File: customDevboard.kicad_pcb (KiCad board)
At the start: 4 copper layers, 40 x 81 mm, 76 parts, among them J1 From BEC, J2 USB_C_Receptacle_USB2.0_14P, J3 From BEC, J4 From Battery, U1 DPS310, U3 TPD2EUSB30, U4 TPS5430DDA, U5 STM32F722RET6, U6 TLV75733PDRV, U7 BMI270, Y1 8MHz, Y2 32.768KHz

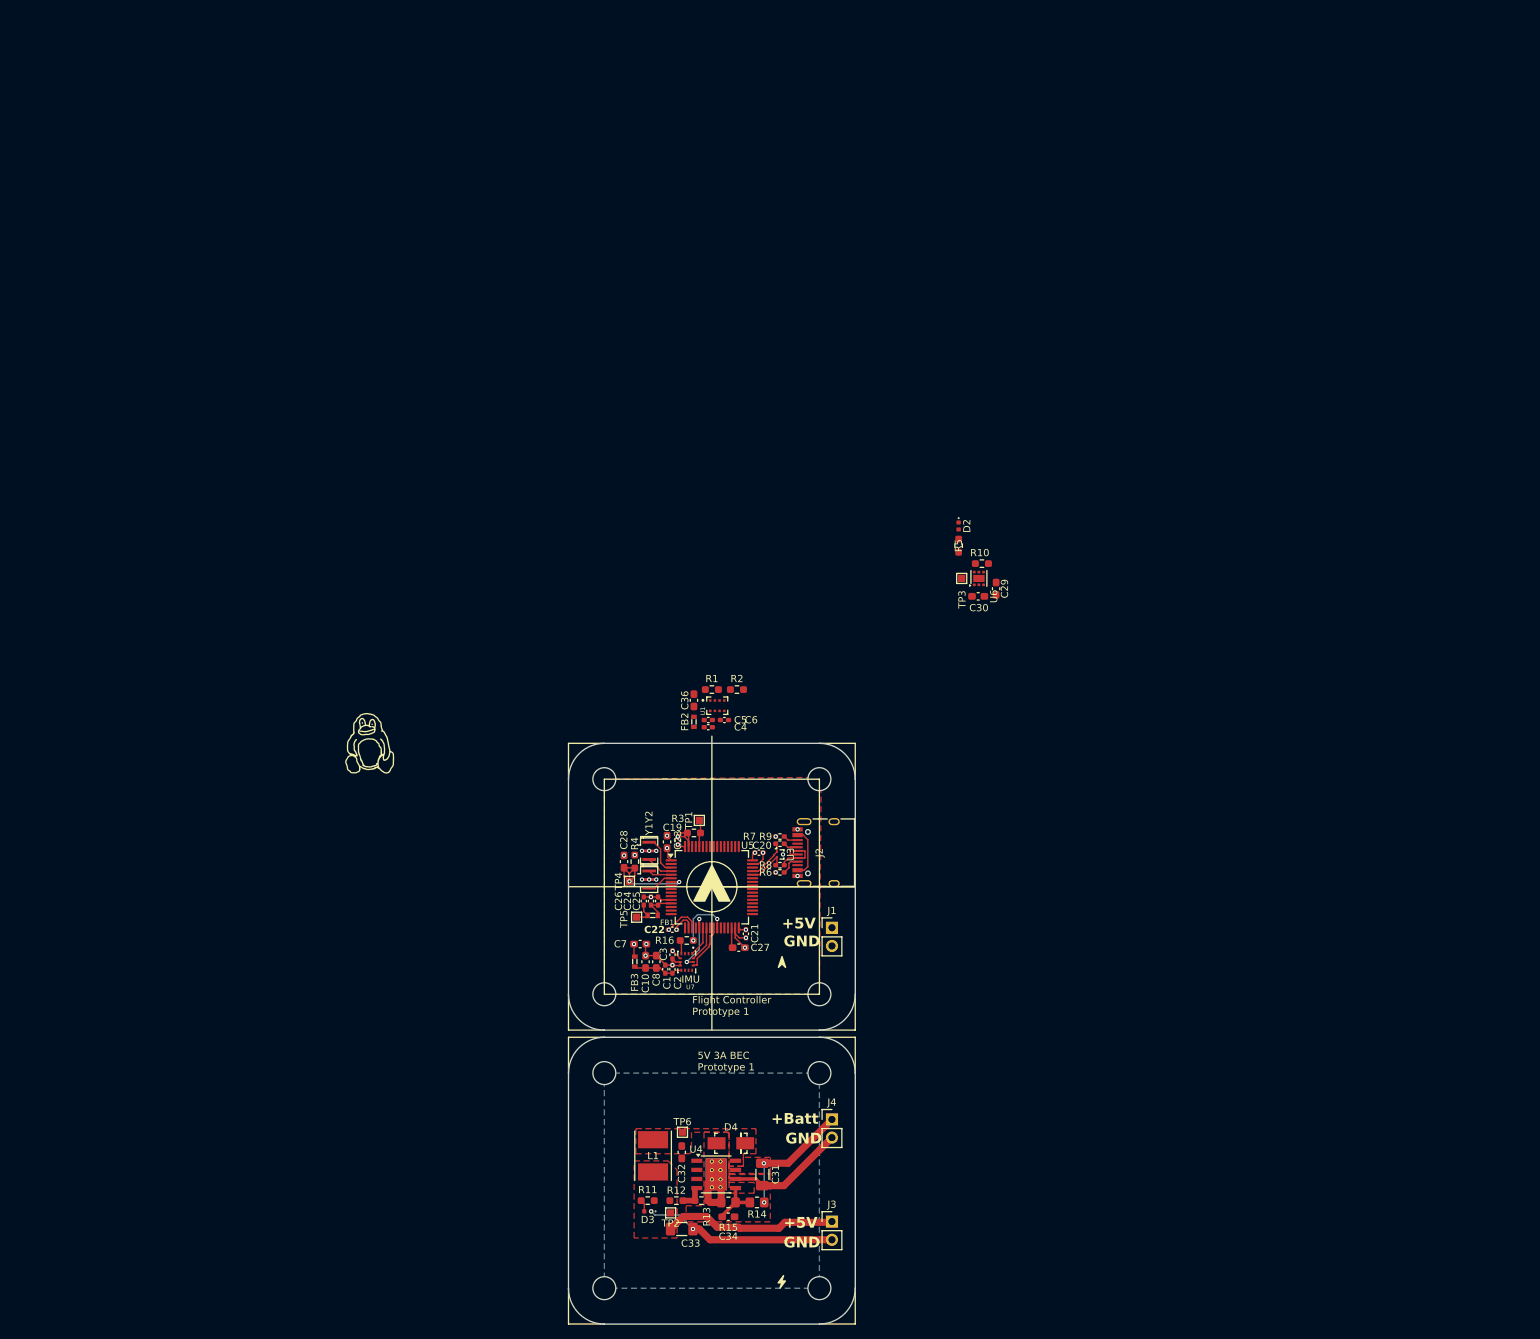
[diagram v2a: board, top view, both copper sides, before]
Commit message: prepare to move esc, gps, bec to other project
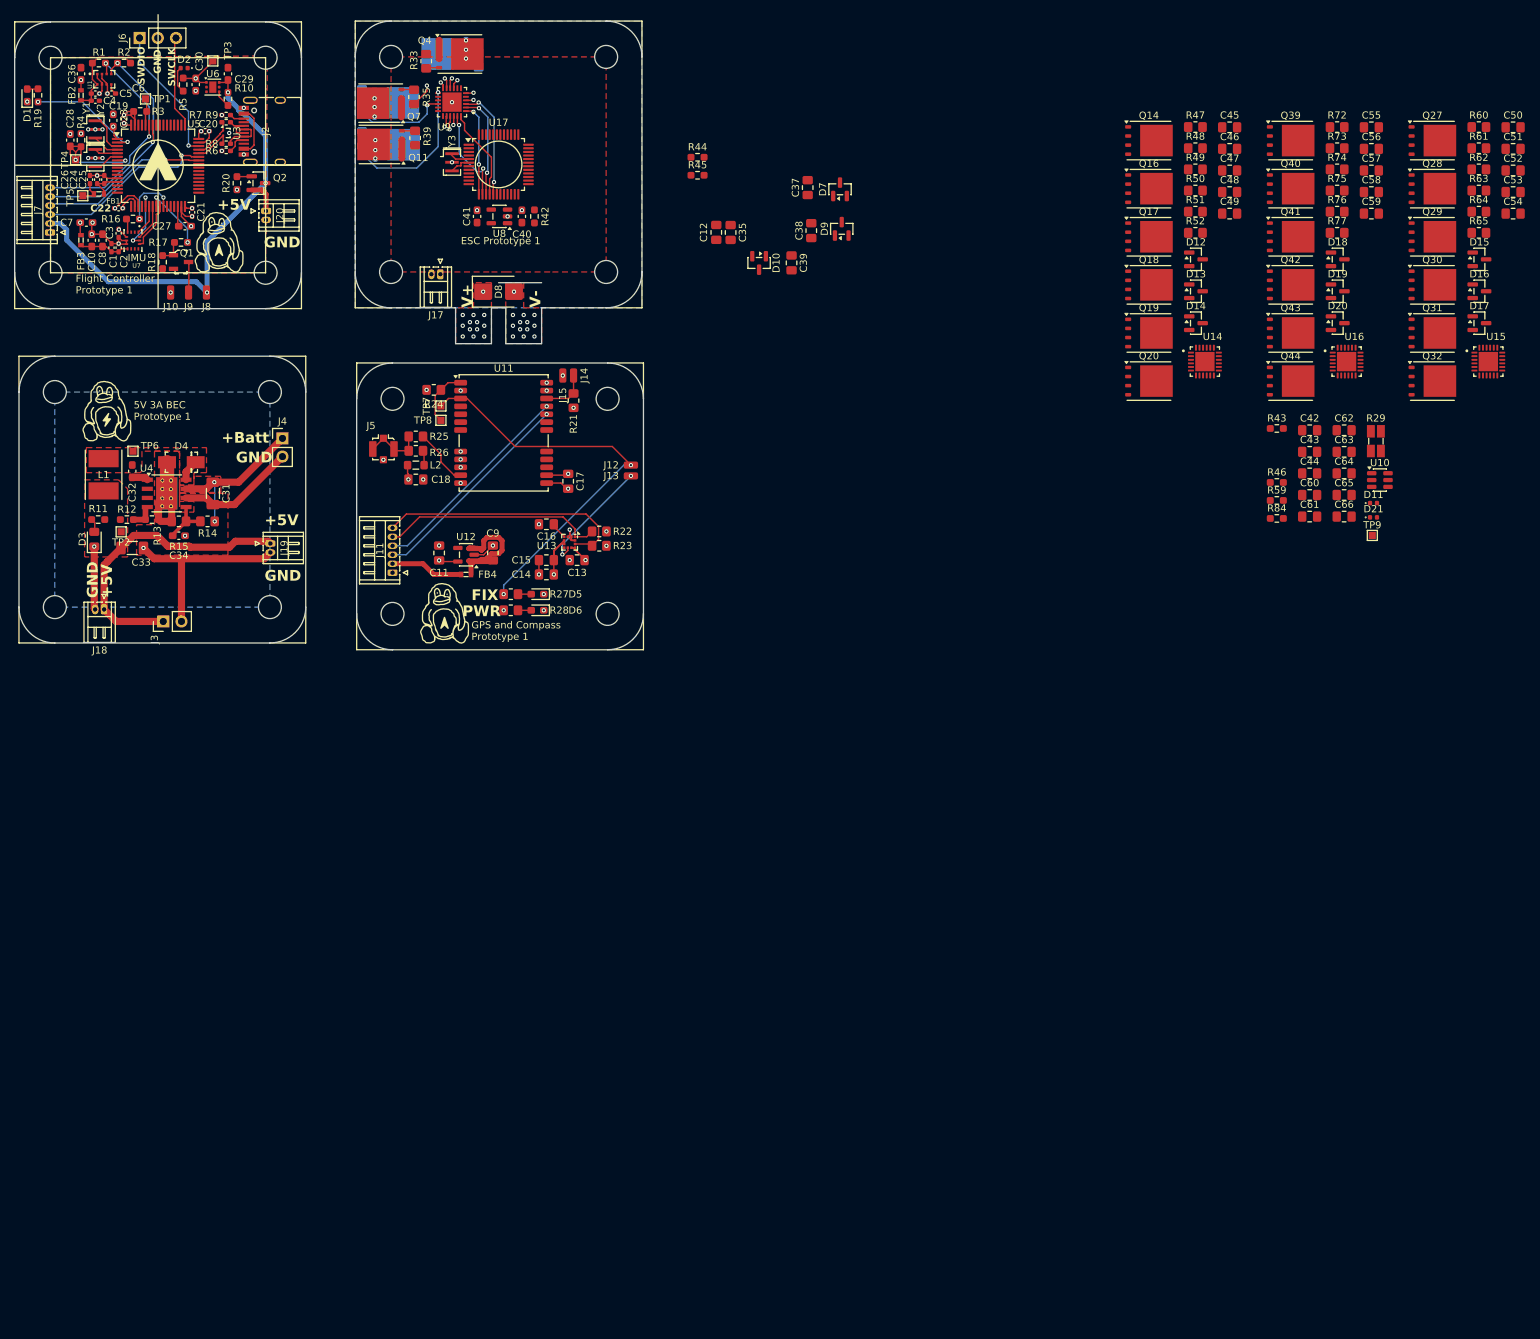
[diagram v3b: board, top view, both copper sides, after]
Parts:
- removed J1: From BEC, Connector_PinHeader_2.54mm:PinHeader_1x02_P2.54mm_Vertical
- added C11: 1uF, Capacitor_SMD:C_0805_2012Metric_Pad1.18x1.45mm_HandSolder, F.Cu at (74.5, 89.4)
- added C12: 10uF, Capacitor_SMD:C_0805_2012Metric_Pad1.18x1.45mm_HandSolder, F.Cu at (113.1, 44.7)
- added C13: 100nF, Capacitor_SMD:C_0805_2012Metric_Pad1.18x1.45mm_HandSolder, F.Cu at (93.7, 90.4)
- added C14: 1uF, Capacitor_SMD:C_0805_2012Metric_Pad1.18x1.45mm_HandSolder, F.Cu at (89.4, 92.4)
- added C15: 100nF, Capacitor_SMD:C_0805_2012Metric_Pad1.18x1.45mm_HandSolder, F.Cu at (89.4, 90.4)
- added C16: 10nF, Capacitor_SMD:C_0805_2012Metric_Pad1.18x1.45mm_HandSolder, F.Cu at (89.4, 85.4)
- added C17: 100nF, Capacitor_SMD:C_0805_2012Metric_Pad1.18x1.45mm_HandSolder, F.Cu at (92.5, 79.4)
- added C18: 100nF, Capacitor_SMD:C_0805_2012Metric_Pad1.18x1.45mm_HandSolder, F.Cu at (71.2, 79.2)
- added C35: 100nF, Capacitor_SMD:C_0805_2012Metric_Pad1.18x1.45mm_HandSolder, F.Cu at (115.1, 44.7)
- added C37: 220nF, Capacitor_SMD:C_0805_2012Metric_Pad1.18x1.45mm_HandSolder, F.Cu at (125.9, 38.5)
- added C38: 220nF, Capacitor_SMD:C_0805_2012Metric_Pad1.18x1.45mm_HandSolder, F.Cu at (126.4, 44.5)
- added C39: 220nF, Capacitor_SMD:C_0805_2012Metric_Pad1.18x1.45mm_HandSolder, F.Cu at (123.6, 49.0)
- added C40: 1uF, Capacitor_SMD:C_0603_1608Metric_Pad1.08x0.95mm_HandSolder, F.Cu at (86.0, 42.5)
- added C41: 2.2uF, Capacitor_SMD:C_0603_1608Metric_Pad1.08x0.95mm_HandSolder, F.Cu at (79.8, 42.5)
- added C42: 100nF, Capacitor_SMD:C_0805_2012Metric_Pad1.18x1.45mm_HandSolder, F.Cu at (195.9, 72.3)
- added C43: 100nF, Capacitor_SMD:C_0805_2012Metric_Pad1.18x1.45mm_HandSolder, F.Cu at (195.9, 75.3)
- added C44: 1uF, Capacitor_SMD:C_0805_2012Metric_Pad1.18x1.45mm_HandSolder, F.Cu at (195.9, 78.3)
- added C45: 10uF, Capacitor_SMD:C_0805_2012Metric_Pad1.18x1.45mm_HandSolder, F.Cu at (184.7, 30.1)
- added C46: 100nF, Capacitor_SMD:C_0805_2012Metric_Pad1.18x1.45mm_HandSolder, F.Cu at (184.7, 33.1)
- added C47: 220nF, Capacitor_SMD:C_0805_2012Metric_Pad1.18x1.45mm_HandSolder, F.Cu at (184.7, 36.1)
- added C48: 220nF, Capacitor_SMD:C_0805_2012Metric_Pad1.18x1.45mm_HandSolder, F.Cu at (184.7, 39.1)
- added C49: 220nF, Capacitor_SMD:C_0805_2012Metric_Pad1.18x1.45mm_HandSolder, F.Cu at (184.7, 42.1)
- added C50: 10uF, Capacitor_SMD:C_0805_2012Metric_Pad1.18x1.45mm_HandSolder, F.Cu at (224.3, 30.1)
- added C51: 100nF, Capacitor_SMD:C_0805_2012Metric_Pad1.18x1.45mm_HandSolder, F.Cu at (224.3, 33.1)
- added C52: 220nF, Capacitor_SMD:C_0805_2012Metric_Pad1.18x1.45mm_HandSolder, F.Cu at (224.3, 36.1)
- added C53: 220nF, Capacitor_SMD:C_0805_2012Metric_Pad1.18x1.45mm_HandSolder, F.Cu at (224.3, 39.1)
- added C54: 220nF, Capacitor_SMD:C_0805_2012Metric_Pad1.18x1.45mm_HandSolder, F.Cu at (224.3, 42.1)
- added C55: 10uF, Capacitor_SMD:C_0805_2012Metric_Pad1.18x1.45mm_HandSolder, F.Cu at (204.5, 30.1)
- added C56: 100nF, Capacitor_SMD:C_0805_2012Metric_Pad1.18x1.45mm_HandSolder, F.Cu at (204.5, 33.1)
- added C57: 220nF, Capacitor_SMD:C_0805_2012Metric_Pad1.18x1.45mm_HandSolder, F.Cu at (204.5, 36.1)
- added C58: 220nF, Capacitor_SMD:C_0805_2012Metric_Pad1.18x1.45mm_HandSolder, F.Cu at (204.5, 39.1)
- added C59: 220nF, Capacitor_SMD:C_0805_2012Metric_Pad1.18x1.45mm_HandSolder, F.Cu at (204.5, 42.1)
- added C60: 100nF, Capacitor_SMD:C_0805_2012Metric_Pad1.18x1.45mm_HandSolder, F.Cu at (195.9, 81.4)
- added C61: 100nF, Capacitor_SMD:C_0805_2012Metric_Pad1.18x1.45mm_HandSolder, F.Cu at (195.9, 84.4)
- added C62: 100nF, Capacitor_SMD:C_0805_2012Metric_Pad1.18x1.45mm_HandSolder, F.Cu at (200.7, 72.3)
- added C63: 100nF, Capacitor_SMD:C_0805_2012Metric_Pad1.18x1.45mm_HandSolder, F.Cu at (200.7, 75.3)
- added C64: 1uF, Capacitor_SMD:C_0805_2012Metric_Pad1.18x1.45mm_HandSolder, F.Cu at (200.7, 78.3)
- added C65: 100nF, Capacitor_SMD:C_0805_2012Metric_Pad1.18x1.45mm_HandSolder, F.Cu at (200.7, 81.4)
- added C66: 100nF, Capacitor_SMD:C_0805_2012Metric_Pad1.18x1.45mm_HandSolder, F.Cu at (200.7, 84.4)
- added C9: 1uF, Capacitor_SMD:C_0805_2012Metric_Pad1.18x1.45mm_HandSolder, F.Cu at (82.0, 89.4)
- added D1: Status LED, LED_SMD:LED_0603_1608Metric_Pad1.05x0.95mm_HandSolder, F.Cu at (17.0, 25.6)
- added D10: BAS21, Package_TO_SOT_SMD:SOT-23, F.Cu at (119.1, 49.0)
- added D11: 3.3V LED, LED_SMD:LED_0402_1005Metric, F.Cu at (204.8, 82.5)
- added D12: BAS21, Package_TO_SOT_SMD:SOT-23, F.Cu at (180.0, 48.5)
- added D13: BAS21, Package_TO_SOT_SMD:SOT-23, F.Cu at (180.0, 52.9)
- added D14: BAS21, Package_TO_SOT_SMD:SOT-23, F.Cu at (180.0, 57.4)
- added D15: BAS21, Package_TO_SOT_SMD:SOT-23, F.Cu at (219.6, 48.5)
- added D16: BAS21, Package_TO_SOT_SMD:SOT-23, F.Cu at (219.6, 52.9)
- added D17: BAS21, Package_TO_SOT_SMD:SOT-23, F.Cu at (219.6, 57.4)
- added D18: BAS21, Package_TO_SOT_SMD:SOT-23, F.Cu at (199.8, 48.5)
- added D19: BAS21, Package_TO_SOT_SMD:SOT-23, F.Cu at (199.8, 52.9)
- added D20: BAS21, Package_TO_SOT_SMD:SOT-23, F.Cu at (199.8, 57.4)
- added D21: 3.3V LED, LED_SMD:LED_0402_1005Metric, F.Cu at (204.8, 84.5)
- added D5: Status LED, LED_SMD:LED_0603_1608Metric_Pad1.05x0.95mm_HandSolder, F.Cu at (88.2, 95.2)
- added D6: Status LED, LED_SMD:LED_0603_1608Metric_Pad1.05x0.95mm_HandSolder, F.Cu at (88.2, 97.4)
- added D7: BAS21, Package_TO_SOT_SMD:SOT-23, F.Cu at (130.4, 38.7)
- added D8: SM6T22A, Diode_SMD:D_SMB, F.Cu at (82.8, 53.0)
- added D9: BAS21, Package_TO_SOT_SMD:SOT-23, F.Cu at (130.6, 44.2)
- added FB4: BLM18AG601SN1D, digikey-footprints:0603, F.Cu at (78.2, 92.4)
- added G***: LOGO, customimages:linuxpenguin, F.Cu at (75.0, 98.2)
- added G***: LOGO, customimages:linuxpenguin, F.Cu at (27.9, 70.0)
- added G***: LOGO, customimages:linuxpenguin, B.Cu at (82.8, 35.3)
- added J10: Debug, Connector_Wire:SolderWirePad_1x01_SMD_1x2mm, F.Cu at (37.0, 53.1)
- added J11: To FC, Connector_Hirose:Hirose_DF13-06P-1.25DS_1x06_P1.25mm_Horizontal, F.Cu at (68.0, 92.2)
- added J12: TimePulse, Connector_Wire:SolderWirePad_1x01_SMD_1x2mm, F.Cu at (101.2, 77.2)
- added J13: DRDY, Connector_Wire:SolderWirePad_1x01_SMD_1x2mm, F.Cu at (101.2, 78.7)
- added J14: C+, Connector_Wire:SolderWirePad_1x01_SMD_1x2mm, F.Cu at (93.2, 64.7)
- added J15: C-, Connector_Wire:SolderWirePad_1x01_SMD_1x2mm, F.Cu at (91.7, 64.7)
- added J17: From BEC, Connector_Hirose:Hirose_DF13-02P-1.25DS_1x02_P1.25mm_Horizontal, F.Cu at (74.6, 50.6)
- added J18: ESC Logic Power, Connector_Hirose:Hirose_DF13-02P-1.25DS_1x02_P1.25mm_Horizontal, F.Cu at (27.7, 97.3)
- added J19: Flight Controller Power, Connector_Hirose:Hirose_DF13-02P-1.25DS_1x02_P1.25mm_Horizontal, F.Cu at (50.9, 88.1)
- added J20: From BEC, Connector_Hirose:Hirose_DF13-02P-1.25DS_1x02_P1.25mm_Horizontal, F.Cu at (50.3, 41.7)
- added J5: U_FL-R-SMT-1_10_, Connector_Coaxial:U.FL_Molex_MCRF_73412-0110_Vertical, F.Cu at (66.7, 74.9)
- added J6: Debug, Connector_PinHeader_2.54mm:PinHeader_1x03_P2.54mm_Vertical, F.Cu at (32.7, 17.6)
- added J7: To GPS, Connector_Hirose:Hirose_DF13-06P-1.25DS_1x06_P1.25mm_Horizontal, F.Cu at (20.2, 44.7)
- added J8: BZ+, Connector_Wire:SolderWirePad_1x01_SMD_1x2mm, F.Cu at (42.0, 53.1)
- added J9: COL, Connector_Wire:SolderWirePad_1x01_SMD_1x2mm, F.Cu at (39.5, 53.1)
- added L2: 10nH, Inductor_SMD:L_0805_2012Metric_Pad1.05x1.20mm_HandSolder, F.Cu at (71.2, 77.2)
- added Q1: BC817, digikey-footprints:SOT-23-3, F.Cu at (38.5, 48.9)
- added Q10: FDMS8350LET40, Package_TO_SOT_SMD:TDSON-8-1, B.Cu at (68.5, 32.5)
- added Q11: FDMS8350LET40, Package_TO_SOT_SMD:TDSON-8-1, F.Cu at (66.3, 32.5)
- added Q14: FDMS8350LET40, Package_TO_SOT_SMD:TDSON-8-1, F.Cu at (173.5, 31.9)
- added Q15: FDMS8350LET40, Package_TO_SOT_SMD:TDSON-8-1, B.Cu at (75.3, 19.9)
- added Q16: FDMS8350LET40, Package_TO_SOT_SMD:TDSON-8-1, F.Cu at (173.5, 38.6)
- added Q17: FDMS8350LET40, Package_TO_SOT_SMD:TDSON-8-1, F.Cu at (173.5, 45.3)
- added Q18: FDMS8350LET40, Package_TO_SOT_SMD:TDSON-8-1, F.Cu at (173.5, 52.0)
- added Q19: FDMS8350LET40, Package_TO_SOT_SMD:TDSON-8-1, F.Cu at (173.5, 58.8)
- added Q2: AO3401A, Package_TO_SOT_SMD:SOT-23, F.Cu at (49.2, 37.9)
- added Q20: FDMS8350LET40, Package_TO_SOT_SMD:TDSON-8-1, F.Cu at (173.5, 65.5)
- added Q27: FDMS8350LET40, Package_TO_SOT_SMD:TDSON-8-1, F.Cu at (213.0, 31.9)
- added Q28: FDMS8350LET40, Package_TO_SOT_SMD:TDSON-8-1, F.Cu at (213.0, 38.6)
- added Q29: FDMS8350LET40, Package_TO_SOT_SMD:TDSON-8-1, F.Cu at (213.0, 45.3)
- added Q30: FDMS8350LET40, Package_TO_SOT_SMD:TDSON-8-1, F.Cu at (213.0, 52.0)
- added Q31: FDMS8350LET40, Package_TO_SOT_SMD:TDSON-8-1, F.Cu at (213.0, 58.8)
- added Q32: FDMS8350LET40, Package_TO_SOT_SMD:TDSON-8-1, F.Cu at (213.0, 65.5)
- added Q39: FDMS8350LET40, Package_TO_SOT_SMD:TDSON-8-1, F.Cu at (193.2, 31.9)
- added Q4: FDMS8350LET40, Package_TO_SOT_SMD:TDSON-8-1, F.Cu at (77.3, 19.9)
- added Q40: FDMS8350LET40, Package_TO_SOT_SMD:TDSON-8-1, F.Cu at (193.2, 38.6)
- added Q41: FDMS8350LET40, Package_TO_SOT_SMD:TDSON-8-1, F.Cu at (193.2, 45.3)
- added Q42: FDMS8350LET40, Package_TO_SOT_SMD:TDSON-8-1, F.Cu at (193.2, 52.0)
- added Q43: FDMS8350LET40, Package_TO_SOT_SMD:TDSON-8-1, F.Cu at (193.2, 58.8)
- added Q44: FDMS8350LET40, Package_TO_SOT_SMD:TDSON-8-1, F.Cu at (193.2, 65.5)
- added Q6: FDMS8350LET40, Package_TO_SOT_SMD:TDSON-8-1, B.Cu at (68.3, 26.7)
- added Q7: FDMS8350LET40, Package_TO_SOT_SMD:TDSON-8-1, F.Cu at (66.3, 26.7)
- added R17: 1k, Resistor_SMD:R_0603_1608Metric_Pad0.98x0.95mm_HandSolder, F.Cu at (38.5, 46.1)
- added R18: 10k, Resistor_SMD:R_0603_1608Metric_Pad0.98x0.95mm_HandSolder, F.Cu at (35.9, 48.9)
- added R19: 1K, Resistor_SMD:R_0603_1608Metric_Pad0.98x0.95mm_HandSolder, F.Cu at (18.5, 25.6)
- added R20: 100k, Resistor_SMD:R_0603_1608Metric_Pad0.98x0.95mm_HandSolder, F.Cu at (46.2, 37.9)
- added R21: 100, Resistor_SMD:R_0805_2012Metric_Pad1.20x1.40mm_HandSolder, F.Cu at (93.2, 68.2)
- added R22: 47, Resistor_SMD:R_0805_2012Metric_Pad1.20x1.40mm_HandSolder, F.Cu at (96.8, 86.4)
- added R23: 47, Resistor_SMD:R_0805_2012Metric_Pad1.20x1.40mm_HandSolder, F.Cu at (96.8, 88.4)
- added R24: 10k, Resistor_SMD:R_0805_2012Metric_Pad1.20x1.40mm_HandSolder, F.Cu at (73.7, 66.7)
- added R25: 0, Resistor_SMD:R_0805_2012Metric_Pad1.20x1.40mm_HandSolder, F.Cu at (71.2, 73.2)
- added R26: 0, Resistor_SMD:R_0805_2012Metric_Pad1.20x1.40mm_HandSolder, F.Cu at (71.2, 75.2)
- added R27: 1K, Resistor_SMD:R_0805_2012Metric_Pad1.20x1.40mm_HandSolder, F.Cu at (84.5, 95.2)
- added R28: 1K, Resistor_SMD:R_0805_2012Metric_Pad1.20x1.40mm_HandSolder, F.Cu at (84.5, 97.4)
- added R29: 0.5m, Resistor_SMD:R_Shunt_Ohmite_LVK12, F.Cu at (205.1, 73.8)
- added R32: 10, Resistor_SMD:R_0805_2012Metric_Pad1.20x1.40mm_HandSolder, B.Cu at (80.0, 20.7)
- added R33: 10, Resistor_SMD:R_0805_2012Metric_Pad1.20x1.40mm_HandSolder, F.Cu at (72.7, 20.9)
- added R34: 10, Resistor_SMD:R_0805_2012Metric_Pad1.20x1.40mm_HandSolder, B.Cu at (63.7, 25.8)
- added R35: 10, Resistor_SMD:R_0805_2012Metric_Pad1.20x1.40mm_HandSolder, F.Cu at (71.0, 25.8)
- added R38: 10, Resistor_SMD:R_0805_2012Metric_Pad1.20x1.40mm_HandSolder, B.Cu at (63.7, 31.6)
- added R39: 10, Resistor_SMD:R_0805_2012Metric_Pad1.20x1.40mm_HandSolder, F.Cu at (71.1, 31.6)
- added R42: 100k, Resistor_SMD:R_0603_1608Metric_Pad0.98x0.95mm_HandSolder, F.Cu at (87.8, 42.5)
- added R43: 10K, Resistor_SMD:R_0603_1608Metric_Pad0.98x0.95mm_HandSolder, F.Cu at (191.3, 72.1)
- added R44: 50k, Resistor_SMD:R_0603_1608Metric_Pad0.98x0.95mm_HandSolder, F.Cu at (110.5, 34.2)
- added R45: 10k, Resistor_SMD:R_0603_1608Metric_Pad0.98x0.95mm_HandSolder, F.Cu at (110.5, 36.8)
- added R46: 10k, Resistor_SMD:R_0603_1608Metric_Pad0.98x0.95mm_HandSolder, F.Cu at (191.3, 79.6)
- added R47: 10, Resistor_SMD:R_0805_2012Metric_Pad1.20x1.40mm_HandSolder, F.Cu at (179.9, 30.0)
- added R48: 10, Resistor_SMD:R_0805_2012Metric_Pad1.20x1.40mm_HandSolder, F.Cu at (179.9, 33.0)
- added R49: 10, Resistor_SMD:R_0805_2012Metric_Pad1.20x1.40mm_HandSolder, F.Cu at (179.9, 35.9)
- added R50: 10, Resistor_SMD:R_0805_2012Metric_Pad1.20x1.40mm_HandSolder, F.Cu at (179.9, 38.9)
- added R51: 10, Resistor_SMD:R_0805_2012Metric_Pad1.20x1.40mm_HandSolder, F.Cu at (179.9, 41.8)
- added R52: 10, Resistor_SMD:R_0805_2012Metric_Pad1.20x1.40mm_HandSolder, F.Cu at (179.9, 44.8)
- added R59: 10k, Resistor_SMD:R_0603_1608Metric_Pad0.98x0.95mm_HandSolder, F.Cu at (191.3, 82.1)
- added R60: 10, Resistor_SMD:R_0805_2012Metric_Pad1.20x1.40mm_HandSolder, F.Cu at (219.5, 30.0)
- added R61: 10, Resistor_SMD:R_0805_2012Metric_Pad1.20x1.40mm_HandSolder, F.Cu at (219.5, 33.0)
- added R62: 10, Resistor_SMD:R_0805_2012Metric_Pad1.20x1.40mm_HandSolder, F.Cu at (219.5, 35.9)
- added R63: 10, Resistor_SMD:R_0805_2012Metric_Pad1.20x1.40mm_HandSolder, F.Cu at (219.5, 38.9)
- added R64: 10, Resistor_SMD:R_0805_2012Metric_Pad1.20x1.40mm_HandSolder, F.Cu at (219.5, 41.8)
- added R65: 10, Resistor_SMD:R_0805_2012Metric_Pad1.20x1.40mm_HandSolder, F.Cu at (219.5, 44.8)
- added R72: 10, Resistor_SMD:R_0805_2012Metric_Pad1.20x1.40mm_HandSolder, F.Cu at (199.7, 30.0)
- added R73: 10, Resistor_SMD:R_0805_2012Metric_Pad1.20x1.40mm_HandSolder, F.Cu at (199.7, 33.0)
- added R74: 10, Resistor_SMD:R_0805_2012Metric_Pad1.20x1.40mm_HandSolder, F.Cu at (199.7, 35.9)
- added R75: 10, Resistor_SMD:R_0805_2012Metric_Pad1.20x1.40mm_HandSolder, F.Cu at (199.7, 38.9)
- added R76: 10, Resistor_SMD:R_0805_2012Metric_Pad1.20x1.40mm_HandSolder, F.Cu at (199.7, 41.8)
- added R77: 10, Resistor_SMD:R_0805_2012Metric_Pad1.20x1.40mm_HandSolder, F.Cu at (199.7, 44.8)
- added R84: 10K, Resistor_SMD:R_0603_1608Metric_Pad0.98x0.95mm_HandSolder, F.Cu at (191.3, 84.6)
- added REF**: MountingHole_3.2mm_M3, MountingHole:MountingHole_3.2mm_M3, F.Cu at (98.0, 67.9)
- added REF**: MountingHole_3.2mm_M3, MountingHole:MountingHole_3.2mm_M3, F.Cu at (68.0, 97.9)
- added REF**: MountingHole_3.2mm_M3, MountingHole:MountingHole_3.2mm_M3, F.Cu at (97.8, 20.2)
- added REF**: MountingHole_3.2mm_M3, MountingHole:MountingHole_3.2mm_M3, F.Cu at (68.0, 67.9)
- added REF**: MountingHole_3.2mm_M3, MountingHole:MountingHole_3.2mm_M3, F.Cu at (67.8, 50.2)
- added REF**: MountingHole_3.2mm_M3, MountingHole:MountingHole_3.2mm_M3, F.Cu at (98.0, 97.9)
- added REF**: MountingHole_3.2mm_M3, MountingHole:MountingHole_3.2mm_M3, F.Cu at (97.8, 50.2)
- added REF**: MountingHole_3.2mm_M3, MountingHole:MountingHole_3.2mm_M3, F.Cu at (67.8, 20.2)
- added TP7: TimePulse, TestPoint:TestPoint_Pad_1.0x1.0mm, F.Cu at (74.7, 68.9)
- added TP8: SAFEBOOT, TestPoint:TestPoint_Pad_1.0x1.0mm, F.Cu at (74.7, 70.9)
- added TP9: +3.3V, TestPoint:TestPoint_Pad_1.0x1.0mm, F.Cu at (204.6, 87.0)
- added U10: INA181, Package_TO_SOT_SMD:SOT-23-6, F.Cu at (205.7, 79.3)
- added U11: NEO-M8N, RF_GPS:ublox_NEO, F.Cu at (83.5, 72.7)
- added U12: TLV75733PDBV, Package_TO_SOT_SMD:SOT-23-5, F.Cu at (78.2, 89.7)
- added U13: LIS3MDL, Package_LGA:LGA-12_2x2mm_P0.5mm, F.Cu at (92.7, 87.9)
- added U14: FD6288Q, FD6288Q:QFN50P400X400X90-25N, F.Cu at (181.3, 62.8)
- added U15: FD6288Q, FD6288Q:QFN50P400X400X90-25N, F.Cu at (220.8, 62.8)
- added U16: FD6288Q, FD6288Q:QFN50P400X400X90-25N, F.Cu at (201.0, 62.8)
- added U17: STM32F303C8T6, Package_QFP:LQFP-48_7x7mm_P0.5mm, F.Cu at (82.8, 35.2)
- added U8: TLV75733PDBV, Package_TO_SOT_SMD:SOT-23-5, F.Cu at (82.9, 42.5)
- added U9: FD6288Q, FD6288Q:QFN50P400X400X90-25N, F.Cu at (76.2, 26.6)
- added Y3: 8 MHz, Crystal:Resonator_SMD_Murata_CSTxExxV-3Pin_3.0x1.1mm, F.Cu at (76.2, 35.0)
- D3: footprint LED_SMD:LED_0402_1005Metric -> LED_SMD:LED_0805_2012Metric_Pad1.15x1.40mm_HandSolder
- moved C30 130.4 mm to (40.5, 24.1), turned to -90 degrees
- moved C29 129.0 mm to (45.0, 22.6), turned to 90 degrees
- moved TP3 127.0 mm to (42.9, 20.8)
- moved U6 127.0 mm to (42.9, 24.5), turned to 0 degrees
- moved C1 126.9 mm to (28.8, 46.9)
- moved C10 126.9 mm to (26.0, 45.8)
- moved C19 126.9 mm to (30.5, 28.9)
- moved C2 126.9 mm to (29.8, 46.9)
- moved C20 126.9 mm to (41.8, 30.6)
- moved C21 126.9 mm to (40.0, 41.9)
- moved C22 126.9 mm to (29.8, 41.4)
- moved C23 126.9 mm to (29.0, 29.1)
- moved C24 126.9 mm to (26.8, 37.4)
- moved C25 126.9 mm to (27.8, 37.4)
- moved C26 126.9 mm to (25.8, 37.4)
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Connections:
- net +BATT renamed BEC_VIN
- C31 pad 2: GND -> BEC_GND
- C33 pad 1: +5V -> BEC_OUT
- C33 pad 2: GND -> BEC_GND
- C34 pad 2: GND -> BEC_GND
- D3 pad 1: GND -> BEC_GND
- D4 pad A: GND -> BEC_GND
- J3 pad 1: +5V -> BEC_OUT
- J3 pad 2: GND -> BEC_GND
- J4 pad 2: GND -> BEC_GND
- L1 pad 2: +5V -> BEC_OUT
- R11 pad 1: +5V -> BEC_OUT
- R12 pad 1: +5V -> BEC_OUT
- R13 pad 2: GND -> BEC_GND
- R15 pad 2: GND -> BEC_GND
- TP2 pad 1: +5V -> BEC_OUT
- U4 pad 6: GND -> BEC_GND
- U4 pad 9: GND -> BEC_GND
- U5 pad 2: unconnected-(U5-PC13-Pad2) -> Status_LED
- U5 pad 24: unconnected-(U5-PC4-Pad24) -> Beeper
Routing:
- net BEC_GND: track 0.00 -> 67.5 mm, vias 0 -> 3
- net TimePulse: track 0.00 -> 56.7 mm, vias 0 -> 2
- net GND: track 86.1 -> 37.0 mm, vias 24 -> 26
- net BEC_OUT: track 0.00 -> 41.2 mm
- net +5V: track 24.3 -> 63.4 mm, vias 0 -> 3
- net GPS_SDA: track 0.00 -> 35.8 mm
- net I2C1_SCL: track 0.00 -> 35.1 mm, vias 0 -> 2
- net I2C1_SDA: track 0.00 -> 33.2 mm, vias 0 -> 2
- net GPS_SCL: track 0.00 -> 31.1 mm
- net GPS_TX: track 0.00 -> 29.6 mm, vias 0 -> 1
- net GPS_RX: track 0.00 -> 29.6 mm, vias 0 -> 1
- net USART1_RX: track 0.00 -> 24.9 mm, vias 0 -> 1
- net USART1_TX: track 0.00 -> 23.4 mm, vias 0 -> 1
- net GPS_3.3V: track 0.00 -> 21.8 mm, vias 0 -> 13
- net ESC_M1_PHASE_3_HIGH: track 0.00 -> 21.3 mm, vias 0 -> 1
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- added copper zone on B.Cu, net BEC_GND
- added copper zone on F.Cu, net BEC_GND
- added copper zone on F.Cu, net BEC_OUT
- added copper zone on B.Cu, net ESC_COM
- added copper zone on F.Cu, net ESC_COM
- added copper zone on F.Cu, net ESC_UNSAFE_VBAT+
- added copper zone on F.Cu, net ESC_UNSAFE_VBAT-
- added copper zone on In1.Cu, net GPS_3.3V
- added copper zone on In2.Cu, net GPS_GND
- removed copper zone on F.Cu, net +5V
- removed copper zone on B.Cu, net GND
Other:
- board size 40 x 81 mm -> 87.7 x 87.7 mm
- board text added: "ESC Prototype 1"
- board text added: "FIX"
- board text added: "GPS and Compass Prototype 1"
- board text added: "PWR"
- board text added: "SWCLK"
- board text added: "SWDIO"
- board text added: "V+"
- board text added: "V-"
